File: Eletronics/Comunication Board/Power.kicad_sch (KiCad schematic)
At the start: 8 parts, among them T1 AMS1117/3V3, U1 BATERIA

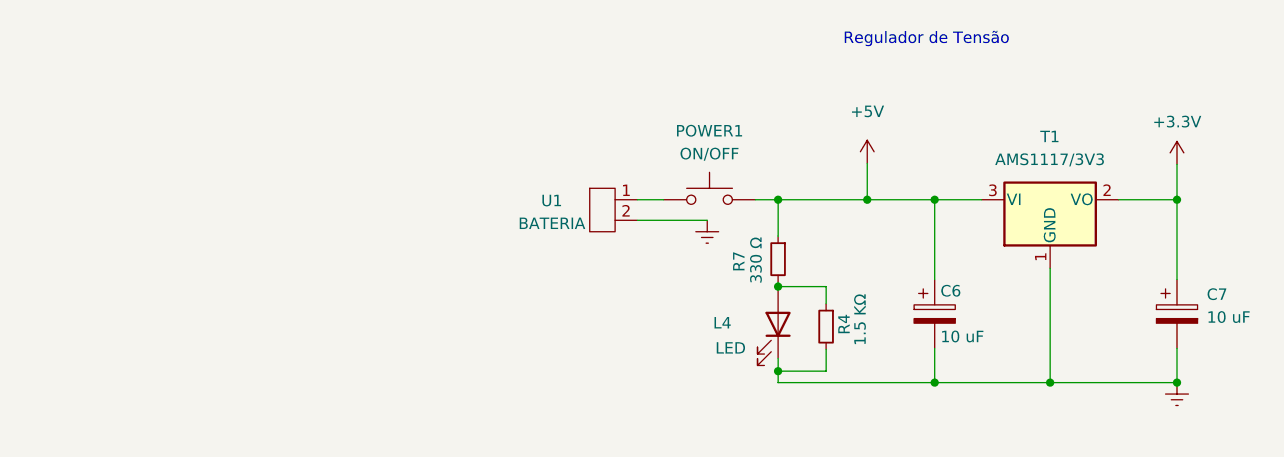
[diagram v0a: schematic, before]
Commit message: Revisão com alterações apontadas no esquemático
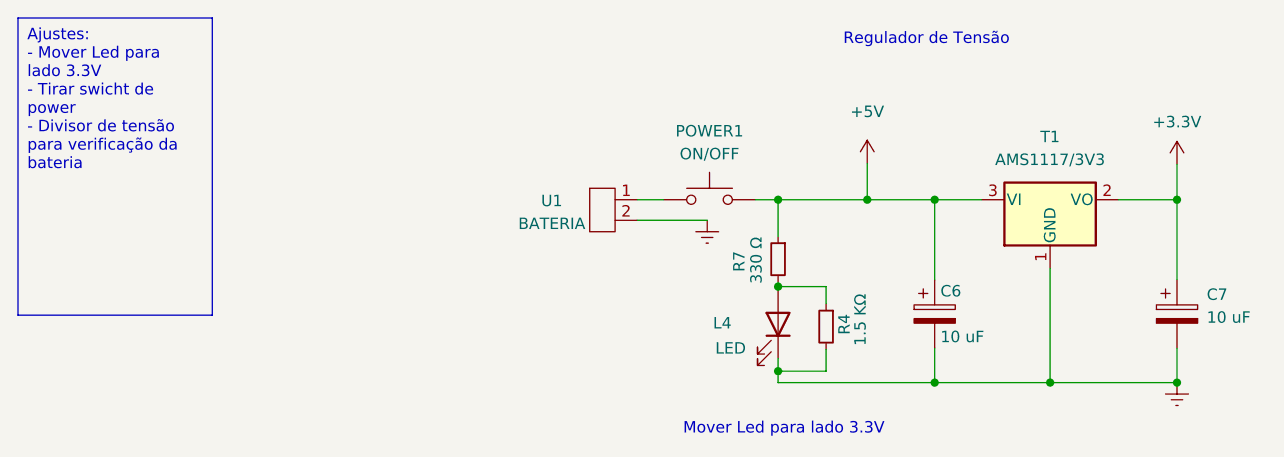
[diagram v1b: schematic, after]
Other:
- note added: "Mover Led para lado 3.3V"
- company: (none) -> Project Neon
- title: (none) -> Placa de comunicação
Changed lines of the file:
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@@
 	(generator_version "8.0")
 	(paper "A4")
+	(title_block
+		(title "Placa de comunicação")
+		(date "2024-05-04")
+		(rev "0")
+		(company "Project Neon")
+		(comment 1 "Autor: Leticia Martins")
+		(comment 2 "Revisão: Marcus Holanda")
+		(comment 3 "Documento com alterações necessárias, não é um docuemnto final")
+	)
 	(junction
 		(at 147.574 96.393)
@@
 		)
 	)
+	(text_box "Ajustes:\n- Mover Led para lado 3.3V\n- Tirar swicht de power\n- Divisor de tensão para verificação da bateria"
+		(exclude_from_sim no)
+		(at 45.72 76.2 0)
+		(size 21.59 33.02)
+		(stroke
+			(width 0)
+			(type default)
+		)
+		(fill
+			(type none)
+		)
+		(effects
+			(font
+				(size 1.27 1.27)
+			)
+			(justify left top)
+		)
+	)
+	(text "Mover Led para lado 3.3V"
+		(exclude_from_sim no)
+		(at 130.81 121.92 0)
+		(effects
+			(font
+				(size 1.27 1.27)
+				(color 255 0 32 1)
+			)
+		)
+	)
